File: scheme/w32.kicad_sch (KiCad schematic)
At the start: 12 parts, among them J5 Micro_SD_Card, U2 W25Q128JVS

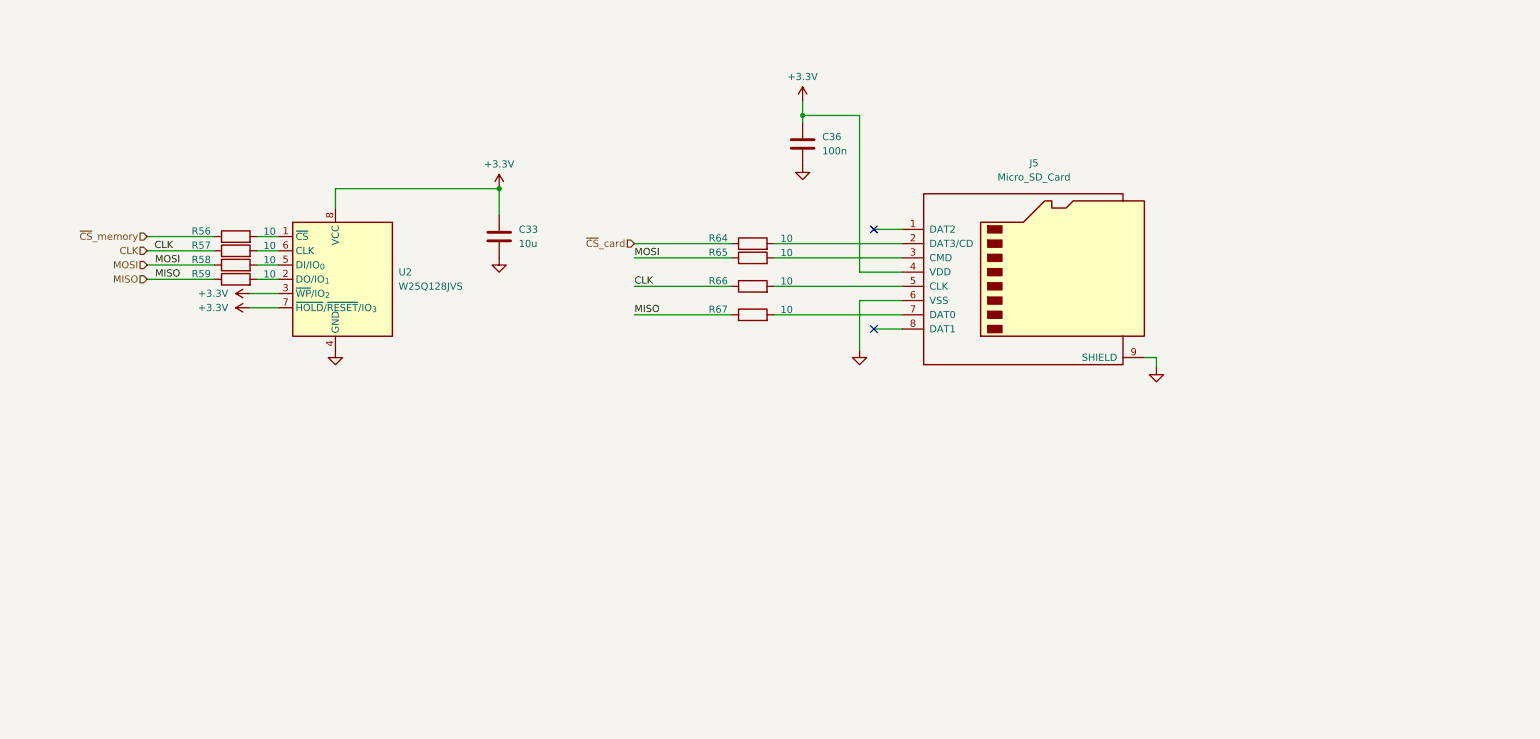
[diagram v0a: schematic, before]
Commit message: feat(schematic): fix peripheral sheets and integrate STM32G0B1CCT6
Главный МК заменён на STM32G0B1CCT6 (LQFP-48, pin-to-pin совместим
с STM32G071CBT6). Лист cpu переписан: обвязка по DS13560, LSE
32.768 кГц, подстроечник на ADC (PA4), перемычка JP_IDD, таблица
назначения выводов.

Исправлены листы периферии:
- st_link: перепутанные USB D+/D-, закороченные резисторы SWD,
  VBUS через PTC и Шоттки, ESD USBLC6-2SC6, LDO AP7361C-33E,
  SWO стянут на землю, J2 1x5 с NRST, перемычка JP_STL_PWR;
- ft232rl: 3V3OUT отвязан от общей шины +3.3V, разделены цепи
  TX/RX и светодиодов, ESD, Шоттки на VBUS, делитель на RESET#;
- w5500: номиналы терминации MDI (49.9 Ом / 10 Ом), PMODE=111,
  RSVD на GND, бусина аналогового питания, подтяжки RST/SCS/INT;
- w32: флэш W25Q32JVSSIQ, символ microSD с детектом карты,
  подтяжки линий SD;
- tmp10x: подтяжки I2C, адреса без резисторов, развязка 100 нФ.

Добавлен лист headers: разъёмы Arduino Uno R3 без ICSP, гребёнки
логического анализатора 1x27 с двух сторон, перемычки JP_SWD.
Удалён пустой лист memory. ERC: 0 ошибок.
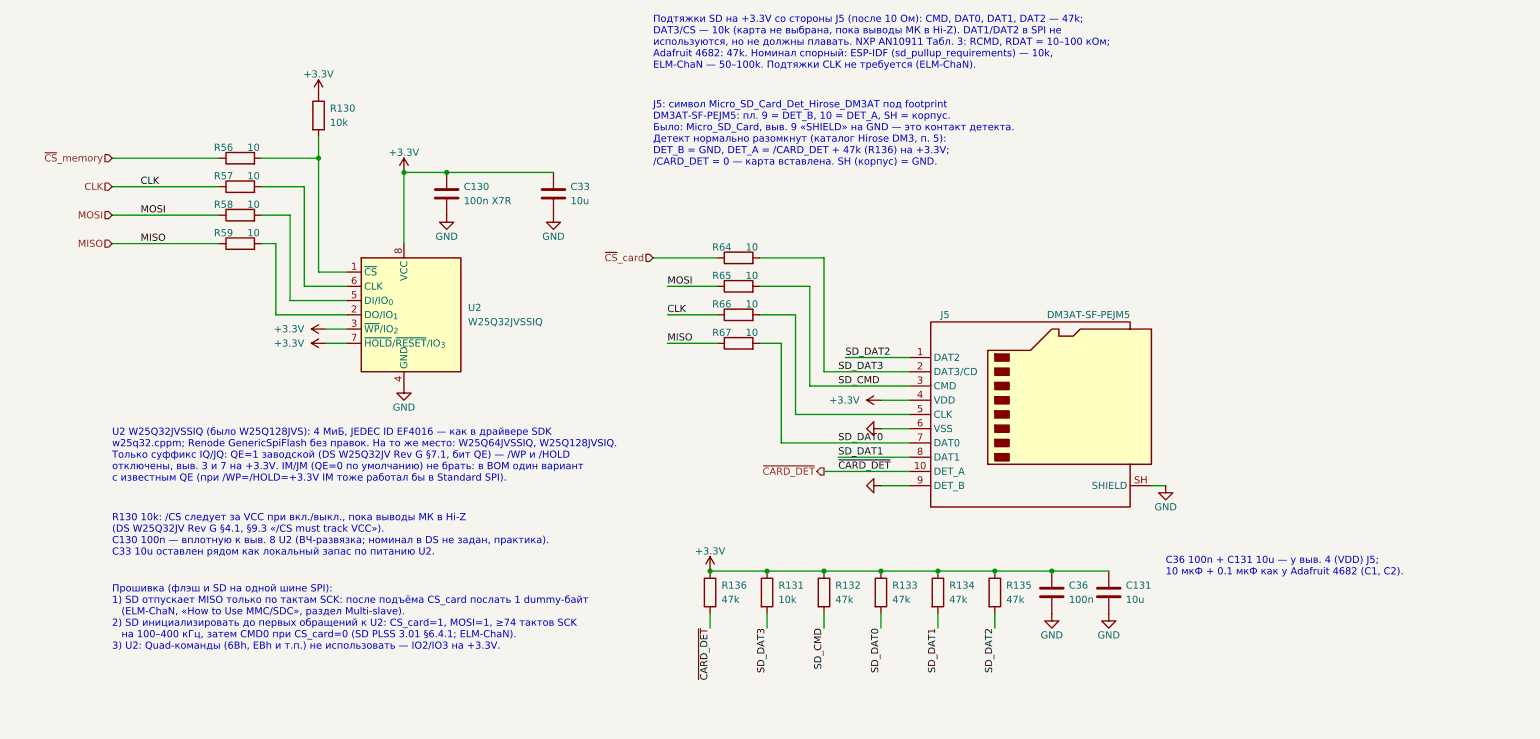
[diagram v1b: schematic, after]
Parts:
- added C130: 100n X7R, Capacitor_SMD:C_0805_2012Metric, symbol Device:C
- added C131: 10u, Capacitor_SMD:C_0805_2012Metric, symbol Device:C
- added R130, R131: 10k, Resistor_SMD:R_0805_2012Metric, symbol Device:R
- added R132, R133, R134, R135, R136: 47k, Resistor_SMD:R_0805_2012Metric, symbol Device:R
- C33, C36: footprint (none) -> Capacitor_SMD:C_0805_2012Metric
- J5: value Micro_SD_Card -> DM3AT-SF-PEJM5; symbol Connector:Micro_SD_Card -> Connector:Micro_SD_Card_Det_Hirose_DM3AT; MPN (none) -> DM3AT-SF-PEJM5
- R56, R57, R58, R59, R64, R65, R66, R67: footprint (none) -> Resistor_SMD:R_0805_2012Metric
- U2: value W25Q128JVS -> W25Q32JVSSIQ; symbol Memory_Flash:W25Q128JVS -> Memory_Flash:W25Q32JVSS; MPN (none) -> W25Q32JVSSIQ
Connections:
- net +3.3V: now also C130.1, C131.1, R130.1, R131.1, R132.1, R133.1, R134.1, R135.1, R136.1
- net GND: now also J5.SH (SHIELD), C130.2, C131.2
- net SD_DAT2: now reaches J5.1 (DAT2)
- net SD_DAT2: now also R135.2
- net SD_DAT3: now reaches J5.2 (DAT3/CD), R64.2
- net SD_DAT3: now also R131.2
- net SD_CMD: now reaches J5.3 (CMD), R65.2
- net SD_CMD: now also R132.2
- net SD_DAT0: now reaches J5.7 (DAT0), R67.2
- net SD_DAT0: now also R133.2
- net SD_DAT1: now reaches J5.8 (DAT1)
- net SD_DAT1: now also R134.2
- net at R56.2, U2.1 (~{CS}): now also R130.2
- new net ~{CARD_DET}: J5.10 (DET_A), R136.2
- no-connect marks 2 -> 0
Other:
- note added: "C36 100n + C131 10u — у выв. 4 (VDD) J5; 10 мкФ + 0.1 мкФ как у Adafruit 4682 (C1, C2)."
- note added: "J5: символ Micro_SD_Card_Det_Hirose_DM3AT под footprint DM3AT-SF-PEJM5: пл. 9 = DET_B, 10 = DET_A, SH = корпус. Было: Micro_SD_Card, выв. 9 «SHIELD» на GND — это контакт детекта. Детект нормально разомкнут (каталог Hirose DM3, п. 5): DET_B = GND, DET_A = /CARD_DET + 47k (R136) на +3.3V; /CARD_DET = 0 — карта вставлена. SH (корпус) = GND."
- note added: "R130 10k: /CS следует за VCC при вкл./выкл., пока выводы МК в Hi-Z (DS W25Q32JV Rev G §4.1, §9.3 «/CS must track VCC»). C130 100n — вплотную к выв. 8 U2 (ВЧ-развязка; номинал в DS не задан, практика). C33 10u оставлен рядом как локальный запас по питанию U2."
- note added: "U2 W25Q32JVSSIQ (было W25Q128JVS): 4 МиБ, JEDEC ID EF4016 — как в драйвере SDK w25q32.cppm; Renode GenericSpiFlash без правок. На то же место: W25Q64JVSSIQ, W25Q128JVSIQ. Только суффикс IQ/JQ: QE=1 заводской (DS W25Q32JV Rev G §7.1, бит QE) — /WP и /HOLD отключены, выв. 3 и 7 на +3.3V. IM/JM (QE=0 по умолчанию) не брать: в BOM один вариант с известным QE (при /WP=/HOLD=+3.3V IM тоже работал бы в 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"
- note added: "Подтяжки SD на +3.3V со стороны J5 (после 10 Ом): CMD, DAT0, DAT1, DAT2 — 47k; DAT3/CS — 10k (карта не выбрана, пока выводы МК в Hi-Z). DAT1/DAT2 в SPI не используются, но не должны плавать. NXP AN10911 Табл. 3: RCMD, RDAT = 10–100 кОм; Adafruit 4682: 47k. Номинал спорный: ESP-IDF (sd_pullup_requirements) — 10k, ELM-ChaN — 50–100k. Подтяжки CLK не требуется (ELM-ChaN)."
- note added: "Прошивка (флэш и SD на одной шине SPI): 1) SD отпускает MISO только по тактам SCK: после подъёма CS_card послать 1 dummy-байт (ELM-ChaN, «How to Use MMC/SDC», раздел Multi-slave). 2) SD инициализировать до первых обращений к U2: CS_card=1, MOSI=1, ≥74 тактов SCK на 100–400 кГц, затем CMD0 при CS_card=0 (SD PLSS 3.01 §6.4.1; ELM-ChaN). 3) U2: Quad-команды (6Bh, EBh и т.п.) не использовать — IO2/IO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"
- moved on the sheet: C33, C36, R56, R57, R58, R59, R64, R65, R66, R67, U2

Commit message: refactor(schematic): re-annotate references by sheet number
Позиционные обозначения перенумерованы по схеме «номер листа x 100»:
cpu - 1xx, st_link - 2xx, ft232rl - 3xx, w5500 - 4xx, w32 - 5xx,
tmp10x - 6xx, leds - 7xx, headers - 8xx. По обозначению на плате
сразу видно, к какому листу относится компонент.

Ссылки на компоненты в текстовых комментариях обновлены. Обозначения
из сторонних референсных схем (MB1136, MB1184, W5500-Ref, Ethernet
Shield, Adafruit) и имена выводов Arduino оставлены без изменений.

Проверено: нетлист до и после совпадает с точностью до переименования
(190 цепей, 187 компонентов), дубликатов нет, ERC - 0 ошибок.
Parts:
- renumbered C130 to C501, C33 to C502, C36 to C503, C131 to C504, J5 to J501, R56 to R501, R57 to R502, R58 to R503, R59 to R504, R130 to R505, R136 to R506, R64 to R507, R65 to R508, R66 to R509, R67 to R510, R131 to R511, R132 to R512, R133 to R513, R134 to R514, R135 to R515, U2 to U501
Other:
- note added: "C503 100n + C504 10u — у выв. 4 (VDD) J501; 10 мкФ + 0.1 мкФ как у Adafruit 4682 (C1, C2)."
- note added: "J501: символ Micro_SD_Card_Det_Hirose_DM3AT под footprint DM3AT-SF-PEJM5: пл. 9 = DET_B, 10 = DET_A, SH = корпус. Было: Micro_SD_Card, выв. 9 «SHIELD» на GND — это контакт детекта. Детект нормально разомкнут (каталог Hirose DM3, п. 5): DET_B = GND, DET_A = /CARD_DET + 47k (R506) на +3.3V; /CARD_DET = 0 — карта вставлена. SH (корпус) = GND."
- note added: "R505 10k: /CS следует за VCC при вкл./выкл., пока выводы МК в Hi-Z (DS W25Q32JV Rev G §4.1, §9.3 «/CS must track VCC»). C501 100n — вплотную к выв. 8 U501 (ВЧ-развязка; номинал в DS не задан, практика). C502 10u оставлен рядом как локальный запас по питанию U501."
- note added: "U501 W25Q32JVSSIQ (было W25Q128JVS): 4 МиБ, JEDEC ID EF4016 — как в драйвере SDK w25q32.cppm; Renode GenericSpiFlash без правок. На то же место: W25Q64JVSSIQ, W25Q128JVSIQ. Только суффикс IQ/JQ: QE=1 заводской (DS W25Q32JV Rev G §7.1, бит QE) — /WP и /HOLD отключены, выв. 3 и 7 на +3.3V. IM/JM (QE=0 по умолчанию) не брать: в BOM один вариант с известным QE (при /WP=/HOLD=+3.3V IM тоже работал бы 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"
- note added: "Подтяжки SD на +3.3V со стороны J501 (после 10 Ом): CMD, DAT0, DAT1, DAT2 — 47k; DAT3/CS — 10k (карта не выбрана, пока выводы МК в Hi-Z). DAT1/DAT2 в SPI не используются, но не должны плавать. NXP AN10911 Табл. 3: RCMD, RDAT = 10–100 кОм; Adafruit 4682: 47k. Номинал спорный: ESP-IDF (sd_pullup_requirements) — 10k, ELM-ChaN — 50–100k. Подтяжки CLK не требуется (ELM-ChaN)."
- note added: "Прошивка (флэш и SD на одной шине SPI): 1) SD отпускает MISO только по тактам SCK: после подъёма CS_card послать 1 dummy-байт (ELM-ChaN, «How to Use MMC/SDC», раздел Multi-slave). 2) SD инициализировать до первых обращений к U501: CS_card=1, MOSI=1, ≥74 тактов SCK на 100–400 кГц, затем CMD0 при CS_card=0 (SD PLSS 3.01 §6.4.1; ELM-ChaN). 3) U501: Quad-команды (6Bh, EBh и т.п.) не использовать — IO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"
- note removed: "C36 100n + C131 10u — у выв. 4 (VDD) J5; 10 мкФ + 0.1 мкФ как у Adafruit 4682 (C1, C2)."
- note removed: "J5: символ Micro_SD_Card_Det_Hirose_DM3AT под footprint DM3AT-SF-PEJM5: пл. 9 = DET_B, 10 = DET_A, SH = корпус. Было: Micro_SD_Card, выв. 9 «SHIELD» на GND — это контакт детекта. Детект нормально разомкнут (каталог Hirose DM3, п. 5): DET_B = GND, DET_A = /CARD_DET + 47k (R136) на +3.3V; /CARD_DET = 0 — карта вставлена. SH (корпус) = GND."
- note removed: "R130 10k: /CS следует за VCC при вкл./выкл., пока выводы МК в Hi-Z (DS W25Q32JV Rev G §4.1, §9.3 «/CS must track VCC»). C130 100n — вплотную к выв. 8 U2 (ВЧ-развязка; номинал в DS не задан, практика). C33 10u оставлен рядом как локальный запас по питанию U2."
- note removed: "U2 W25Q32JVSSIQ (было W25Q128JVS): 4 МиБ, JEDEC ID EF4016 — как в драйвере SDK w25q32.cppm; Renode GenericSpiFlash без правок. На то же место: W25Q64JVSSIQ, W25Q128JVSIQ. Только суффикс IQ/JQ: QE=1 заводской (DS W25Q32JV Rev G §7.1, бит QE) — /WP и /HOLD отключены, выв. 3 и 7 на +3.3V. IM/JM (QE=0 по умолчанию) не брать: в BOM один вариант с известным QE (при /WP=/HOLD=+3.3V IM тоже работал бы в 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"
- note removed: "Подтяжки SD на +3.3V со стороны J5 (после 10 Ом): CMD, DAT0, DAT1, DAT2 — 47k; DAT3/CS — 10k (карта не выбрана, пока выводы МК в Hi-Z). DAT1/DAT2 в SPI не используются, но не должны плавать. NXP AN10911 Табл. 3: RCMD, RDAT = 10–100 кОм; Adafruit 4682: 47k. Номинал спорный: ESP-IDF (sd_pullup_requirements) — 10k, ELM-ChaN — 50–100k. Подтяжки CLK не требуется (ELM-ChaN)."
- note removed: "Прошивка (флэш и SD на одной шине SPI): 1) SD отпускает MISO только по тактам SCK: после подъёма CS_card послать 1 dummy-байт (ELM-ChaN, «How to Use MMC/SDC», раздел Multi-slave). 2) SD инициализировать до первых обращений к U2: CS_card=1, MOSI=1, ≥74 тактов SCK на 100–400 кГц, затем CMD0 при CS_card=0 (SD PLSS 3.01 §6.4.1; ELM-ChaN). 3) U2: Quad-команды (6Bh, EBh и т.п.) не использовать — IO2/IO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"

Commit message: fix(schematic): resolve all ERC warnings
ERC: 0 ошибок, 0 предупреждений (было 239 предупреждений).

- w5500, leds: все объекты перенесены на сетку 1.27 мм; удалены
  два провода нулевой длины.
- Заведена проектная библиотека g0_dev_board.kicad_sym (+ sym-lib-table)
  для намеренно изменённых символов: USB_B_Mini с пассивными
  VBUS/GND (J201, J301). Попутно исправлен номер вывода экрана
  6 -> SH: у footprint Lumberg 2486 01 площадки экрана называются SH,
  иначе экран на плате остался бы неподключённым.
- Устаревшие копии символа LED обновлены из стандартной библиотеки.
- Кнопки SW701/SW702: SW_DPST_x2 заменён на SW_Push, footprint
  SW_SPST_PTS645Sx43SMTR92 (площадки 1,1,2,2 уже попарно замкнуты).
- Флэш U501: WP и HOLD подтянуты к +3.3V через R516/R517 10k
  вместо прямого подключения к выходу LDO.

Связность проверена сравнением нетлистов: изменились только цепи
WP/HOLD флэша.
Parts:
- added R516, R517: 10k, Resistor_SMD:R_0805_2012Metric, symbol Device:R
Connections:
- net +3.3V: now also R516.1, R517.1; no longer U501.3 (~{WP}/IO_{2}), U501.7 (~{HOLD}/~{RESET}/IO_{3})
- new net: R516.2, U501.3 (~{WP}/IO_{2})
- new net: R517.2, U501.7 (~{HOLD}/~{RESET}/IO_{3})
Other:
- note added: "U501 W25Q32JVSSIQ (было W25Q128JVS): 4 МиБ, JEDEC ID EF4016 — как в драйвере SDK w25q32.cppm; Renode GenericSpiFlash без правок. На то же место: W25Q64JVSSIQ, W25Q128JVSIQ. Только суффикс IQ/JQ: QE=1 заводской (DS W25Q32JV Rev G §7.1, бит QE) — /WP и /HOLD отключены. Выв. 3 и 7 — через R516, R517 10k на +3.3V: это I/O (IO2/IO3, DS §3.3, §4.2–4.4), напрямую на шину питания не сажать; номинал 10k в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"
- note removed: "U501 W25Q32JVSSIQ (было W25Q128JVS): 4 МиБ, JEDEC ID EF4016 — как в драйвере SDK w25q32.cppm; Renode GenericSpiFlash без правок. На то же место: W25Q64JVSSIQ, W25Q128JVSIQ. Только суффикс IQ/JQ: QE=1 заводской (DS W25Q32JV Rev G §7.1, бит QE) — /WP и /HOLD отключены, выв. 3 и 7 на +3.3V. IM/JM (QE=0 по умолчанию) не брать: в BOM один вариант с известным QE (при /WP=/HOLD=+3.3V IM тоже работал бы 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"
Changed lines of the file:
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@@
 		)
 	)
-	(text "U501 W25Q32JVSSIQ (было W25Q128JVS): 4 МиБ, JEDEC ID EF4016 — как в драйвере SDK\nw25q32.cppm; Renode GenericSpiFlash без правок. На то же место: W25Q64JVSSIQ, W25Q128JVSIQ.\nТолько суффикс IQ/JQ: QE=1 заводской (DS W25Q32JV Rev G §7.1, бит QE) — /WP и /HOLD\nотключены, выв. 3 и 7 на +3.3V. IM/JM (QE=0 по умолчанию) не брать: в BOM один вариант\nс известным QE (при /WP=/HOLD=+3.3V IM тоже работал бы в Standard SPI)."
+	(text "U501 W25Q32JVSSIQ (было W25Q128JVS): 4 МиБ, JEDEC ID EF4016 — как в драйвере SDK\nw25q32.cppm; Renode GenericSpiFlash без правок. На то же место: W25Q64JVSSIQ, W25Q128JVSIQ.\nТолько суффикс IQ/JQ: QE=1 заводской (DS W25Q32JV Rev G §7.1, бит QE) — /WP и /HOLD\nотключены. Выв. 3 и 7 — через R516, R517 10k на +3.3V: это I/O (IO2/IO3, DS §3.3, §4.2–4.4),\nнапрямую на шину питания не сажать; номинал 10k в DS не задан (практика). IM/JM (QE=0 по умолч.)\nне брать: в BOM один вариант с известным QE (при /WP=/HOLD=1 IM работал бы в Standard SPI)."
 		(exclude_from_sim no)
 		(at 38.1 99.06 0)
@@
 		)
 	)
-	(text "Прошивка (флэш и SD на одной шине SPI):\n1) SD отпускает MISO только по тактам SCK: после подъёма CS_card послать 1 dummy-байт\n   (ELM-ChaN, «How to Use MMC/SDC», раздел Multi-slave).\n2) SD инициализировать до первых обращений к U501: CS_card=1, MOSI=1, ≥74 тактов SCK\n   на 100–400 кГц, затем CMD0 при CS_card=0 (SD PLSS 3.01 §6.4.1; ELM-ChaN).\n3) U501: Quad-команды (6Bh, EBh и т.п.) не использовать — IO2/IO3 на +3.3V."
+	(text "Прошивка (флэш и SD на одной шине SPI):\n1) SD отпускает MISO только по тактам SCK: после подъёма CS_card послать 1 dummy-байт\n   (ELM-ChaN, «How to Use MMC/SDC», раздел Multi-slave).\n2) SD инициализировать до первых обращений к U501: CS_card=1, MOSI=1, ≥74 тактов SCK\n   на 100–400 кГц, затем CMD0 при CS_card=0 (SD PLSS 3.01 §6.4.1; ELM-ChaN).\n3) U501: Quad-команды (6Bh, EBh и т.п.) не использовать — IO2/IO3 подтянуты к +3.3V (R516, R517)."
 		(exclude_from_sim no)
 		(at 38.1 127 0)
@@
 	(wire
 		(pts
-			(xy 76.2 83.82) (xy 80.01 83.82)
-		)
-		(stroke
-			(width 0)
-			(type default)
-		)
-	)
-	(wire
-		(pts
 			(xy 153.67 83.82) (xy 157.48 83.82)
 		)
@@
 		(pts
 			(xy 157.48 101.6) (xy 180.34 101.6)
-		)
-		(stroke
-			(width 0)
-			(type default)
-		)
-	)
-	(wire
-		(pts
-			(xy 76.2 81.28) (xy 80.01 81.28)
 		)
 		(stroke
@@
 	(symbol
 		(lib_id "power:+3.3V")
-		(at 76.2 81.28 90)
+		(at 66.04 81.28 90)
 		(unit 1)
 		(body_style 1)
@@
 		(dnp no)
 		(property "Reference" "#PWR0099"
-			(at 80.01 81.28 90)
+			(at 69.85 81.28 90)
 			(hide yes)
 			(show_name no)
@@
 		)
 		(property "Value" "+3.3V"
-			(at 72.39 81.28 90)
+			(at 62.23 81.28 90)
 			(show_name no)
 			(do_not_autoplace no)
@@
 		)
 		(property "Footprint" ""
-			(at 76.2 81.28 0)
+			(at 66.04 81.28 0)
 			(hide yes)
 			(show_name no)
@@
 		)
 		(property "Datasheet" ""
-			(at 76.2 81.28 0)
+			(at 66.04 81.28 0)
 			(hide yes)
 			(show_name no)
@@
 		)
 		(property "Description" "Power symbol creates a global label with name \\\"+3.3V\\\""
-			(at 76.2 81.28 0)
+			(at 66.04 81.28 0)
 			(hide yes)
 			(show_name no)
@@
 	)
 	(symbol
+		(lib_id "Device:R")
+		(at 69.85 81.28 90)
+		(unit 1)
+		(body_style 1)
+		(exclude_from_sim no)
+		(in_bom yes)
+		(on_board yes)
+		(in_pos_files yes)
+		(dnp no)
+		(property "Reference" "R516"
+			(at 68.58 83.82 90)
+			(show_name no)
+			(do_not_autoplace no)
+			(effects
+				(font
+					(size 1.27 1.27)
+				)
+				(justify left)
+			)
+		)
+		(property "Value" "10k"
+			(at 71.12 83.82 90)
+			(show_name no)
+			(do_not_autoplace no)
+			(effects
+				(font
+					(size 1.27 1.27)
+				)
+				(justify right)
+			)
+		)
+		(property "Footprint" "Resistor_SMD:R_0805_2012Metric"
+			(at 69.85 81.28 0)
+			(hide yes)
+			(show_name no)
+			(do_not_autoplace no)
+			(effects
+				(font
+					(size 1.27 1.27)
+				)
+			)
+		)
+		(property "Datasheet" ""
+			(at 69.85 81.28 0)
+			(hide yes)
+			(show_name no)
+			(do_not_autoplace no)
+			(effects
+				(font
+					(size 1.27 1.27)
+				)
+			)
+		)
+		(property "Description" "Resistor"
+			(at 69.85 81.28 0)
+			(hide yes)
+			(show_name no)
+			(do_not_autoplace no)
+			(effects
+				(font
+					(size 1.27 1.27)
+				)
+			)
+		)
+		(pin "1"
+		)
+		(pin "2"
+		)
+		(instances
+			(project "g0_dev_board"
+				(path "/997acf0a-b54e-4c77-ad84-80f8d6e2dc27/ed829014-e938-4777-adbe-da6a5ed2b55d"
+					(reference "R516")
+					(unit 1)
+				)
+			)
+		)
+	)
+	(symbol
+		(lib_id "Device:R")
+		(at 69.85 88.9 90)
+		(unit 1)
+		(body_style 1)
+		(exclude_from_sim no)
+		(in_bom yes)
+		(on_board yes)
+		(in_pos_files yes)
+		(dnp no)
+		(property "Reference" "R517"
+			(at 68.58 91.44 90)
+			(show_name no)
+			(do_not_autoplace no)
+			(effects
+				(font
+					(size 1.27 1.27)
+				)
+				(justify left)
+			)
+		)
+		(property "Value" "10k"
+			(at 71.12 91.44 90)
+			(show_name no)
+			(do_not_autoplace no)
+			(effects
+				(font
+					(size 1.27 1.27)
+				)
+				(justify right)
+			)
+		)
+		(property "Footprint" "Resistor_SMD:R_0805_2012Metric"
+			(at 69.85 88.9 0)
+			(hide yes)
+			(show_name no)
+			(do_not_autoplace no)
+			(effects
+				(font
+					(size 1.27 1.27)
+				)
+			)
+		)
+		(property "Datasheet" ""
+			(at 69.85 88.9 0)
+			(hide yes)
+			(show_name no)
+			(do_not_autoplace no)
+			(effects
+				(font
+					(size 1.27 1.27)
+				)
+			)
+		)
+		(property "Description" "Resistor"
+			(at 69.85 88.9 0)
+			(hide yes)
+			(show_name no)
+			(do_not_autoplace no)
+			(effects
+				(font
+					(size 1.27 1.27)
+				)
+			)
+		)
+		(pin "1"
+		)
+		(pin "2"
+		)
+		(instances
+			(project "g0_dev_board"
+				(path "/997acf0a-b54e-4c77-ad84-80f8d6e2dc27/ed829014-e938-4777-adbe-da6a5ed2b55d"
+					(reference "R517")
+					(unit 1)
+				)
+			)
+		)
+	)
+	(wire
+		(pts
+			(xy 73.66 81.28) (xy 80.01 81.28)
+		)
+		(stroke
+			(width 0)
+			(type default)
+		)
+	)
+	(wire
+		(pts
+			(xy 80.01 83.82) (xy 76.2 83.82)
+		)
+		(stroke
+			(width 0)
+			(type default)
+		)
+	)
+	(wire
+		(pts
+			(xy 76.2 83.82) (xy 76.2 88.9)
+		)
+		(stroke
+			(width 0)
+			(type default)
+		)
+	)
+	(wire
+		(pts
+			(xy 76.2 88.9) (xy 73.66 88.9)
+		)
+		(stroke
+			(width 0)
+			(type default)
+		)
+	)
+	(symbol
 		(lib_id "Device:C")
 		(at 205.74 128.27 0)
@@
 	(symbol
 		(lib_id "power:+3.3V")
-		(at 76.2 83.82 90)
+		(at 66.04 88.9 90)
 		(unit 1)
 		(body_style 1)
@@
 		(dnp no)
 		(property "Reference" "#PWR0100"
-			(at 80.01 83.82 90)
+			(at 69.85 88.9 90)
 			(hide yes)
 			(show_name no)
@@
 		)
 		(property "Value" "+3.3V"
-			(at 72.39 83.82 90)
+			(at 62.23 88.9 90)
 			(show_name no)
 			(do_not_autoplace no)
@@
 		)
 		(property "Footprint" ""
-			(at 76.2 83.82 0)
+			(at 66.04 88.9 0)
 			(hide yes)
 			(show_name no)
@@
 		)
 		(property "Datasheet" ""
-			(at 76.2 83.82 0)
+			(at 66.04 88.9 0)
 			(hide yes)
 			(show_name no)
@@
 		)
 		(property "Description" "Power symbol creates a global label with name \\\"+3.3V\\\""
-			(at 76.2 83.82 0)
-			(hide yes)
-			(show_name no)
+			(at 66.04 88.9 0)
+			(hide yes)
+			(show_name no)
